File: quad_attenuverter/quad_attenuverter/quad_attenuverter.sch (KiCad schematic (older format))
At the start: 59 parts

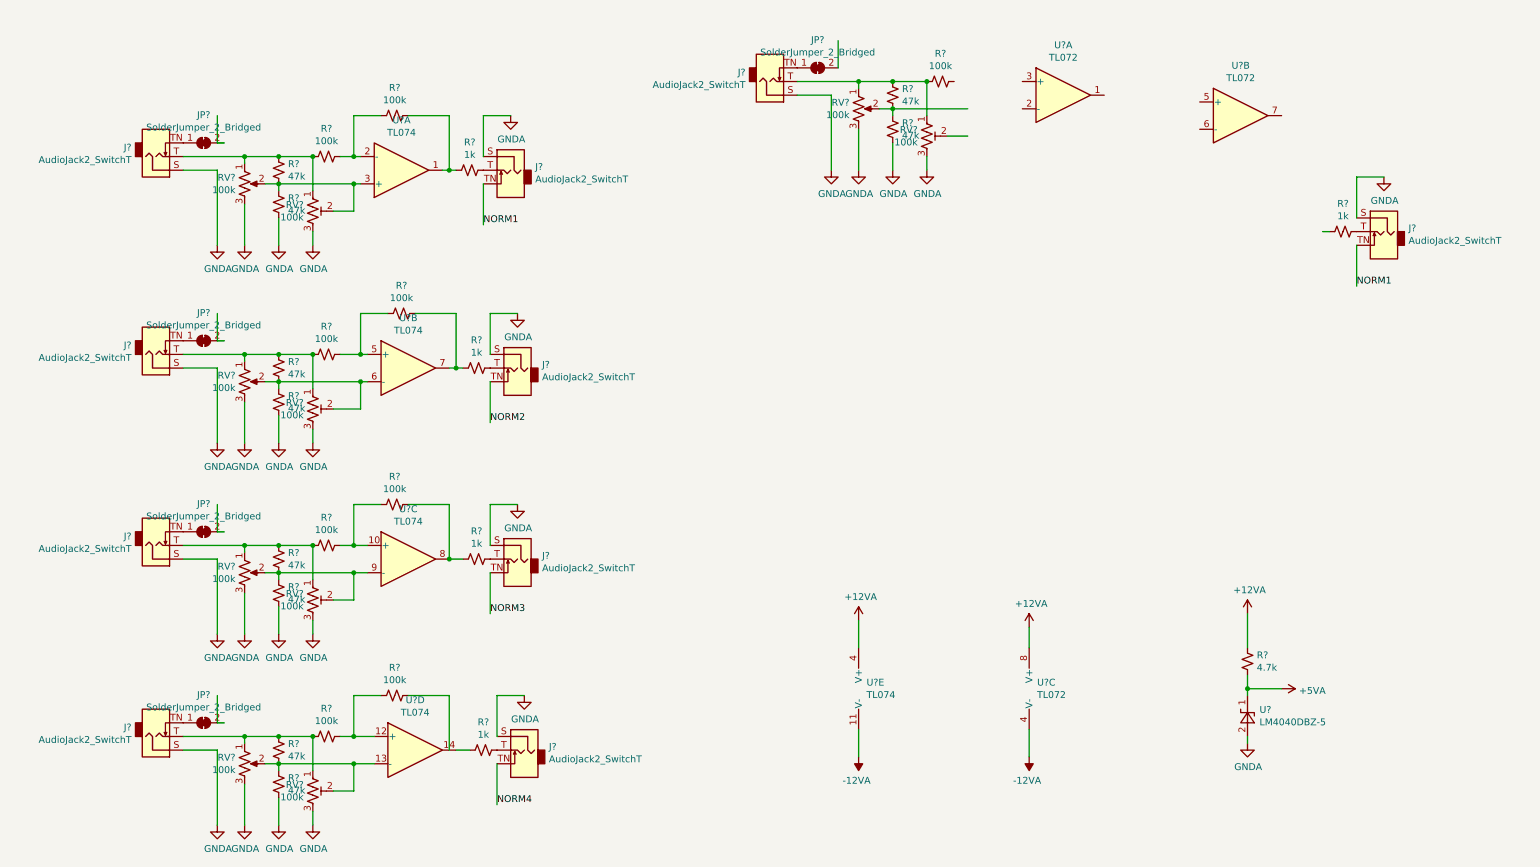
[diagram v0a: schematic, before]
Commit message: Reorganized eurorack modules.
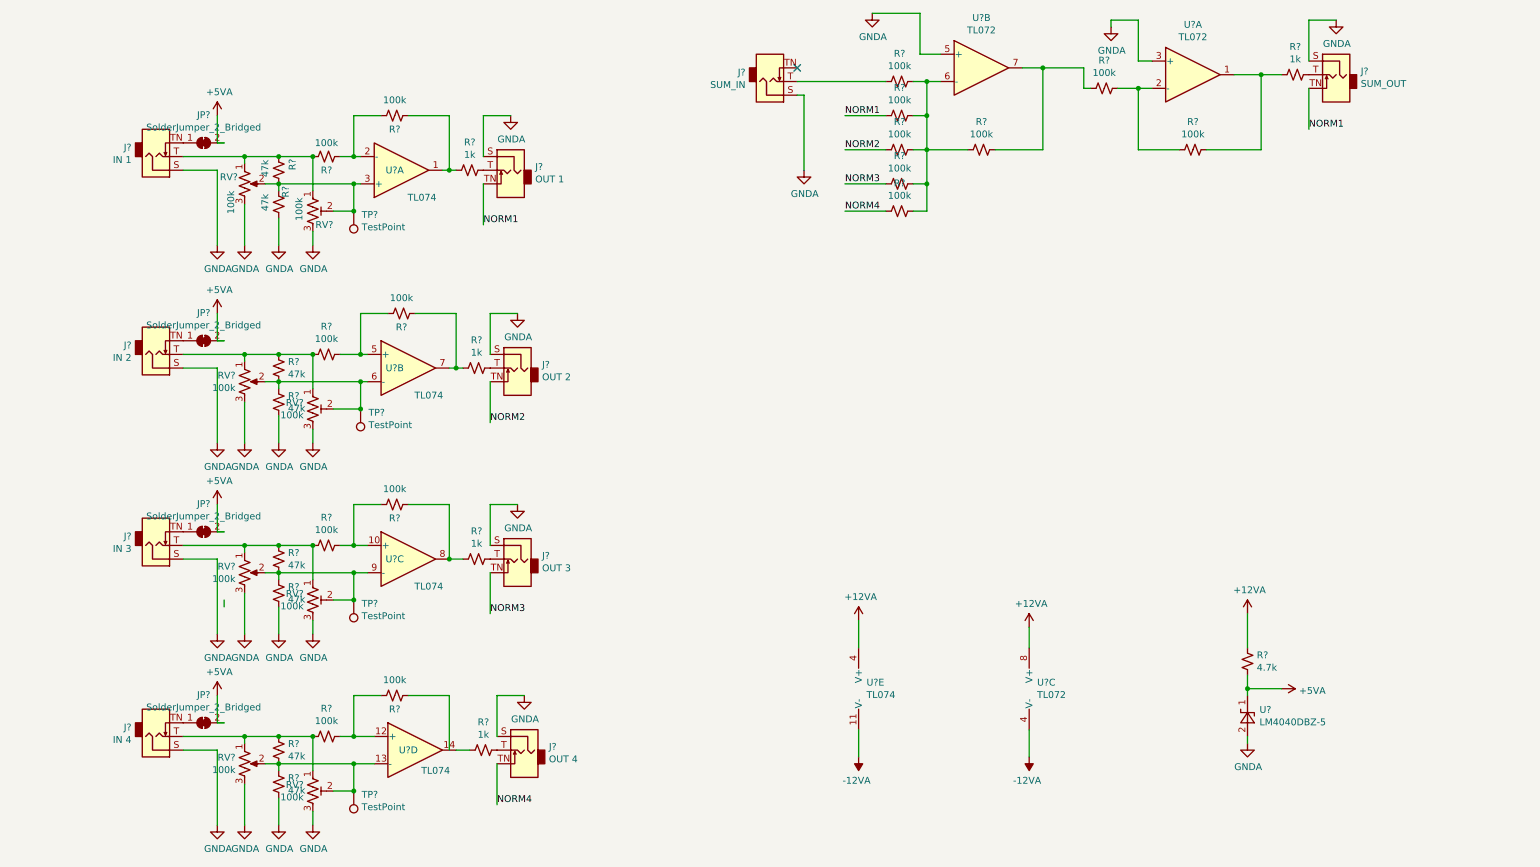
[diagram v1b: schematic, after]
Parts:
- removed JP?: SolderJumper_2_Bridged, symbol Jumper:SolderJumper_2_Bridged
- removed R? (x2): 47k, symbol Device:R_Small_US
- removed RV?: 100k, symbol Device:R_POT_TRIM_US
- removed RV?: 100k, symbol Device:R_POT_US
- added R? (x7): 100k, symbol Device:R_Small_US
- added TP? (x4): TestPoint, symbol Connector:TestPoint
- J?: value AudioJack2_SwitchT -> IN 1
- J?: value AudioJack2_SwitchT -> OUT 1
- J?: value AudioJack2_SwitchT -> OUT 2
- J?: value AudioJack2_SwitchT -> OUT 3
- J?: value AudioJack2_SwitchT -> OUT 4
- J?: value AudioJack2_SwitchT -> SUM_OUT
- J?: value AudioJack2_SwitchT -> IN 4
- J?: value AudioJack2_SwitchT -> IN 2
- J?: value AudioJack2_SwitchT -> SUM_IN
- J?: value AudioJack2_SwitchT -> IN 3
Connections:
- wire segments 142 -> 166
- no-connect marks 0 -> 1
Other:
- moved on the sheet: J?, R?, U?A, U?B
